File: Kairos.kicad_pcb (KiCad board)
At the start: 2 copper layers, 285 x 94.6 mm, 130 parts, among them U1 ATMEGA32U2-AU, Y1 Crystal

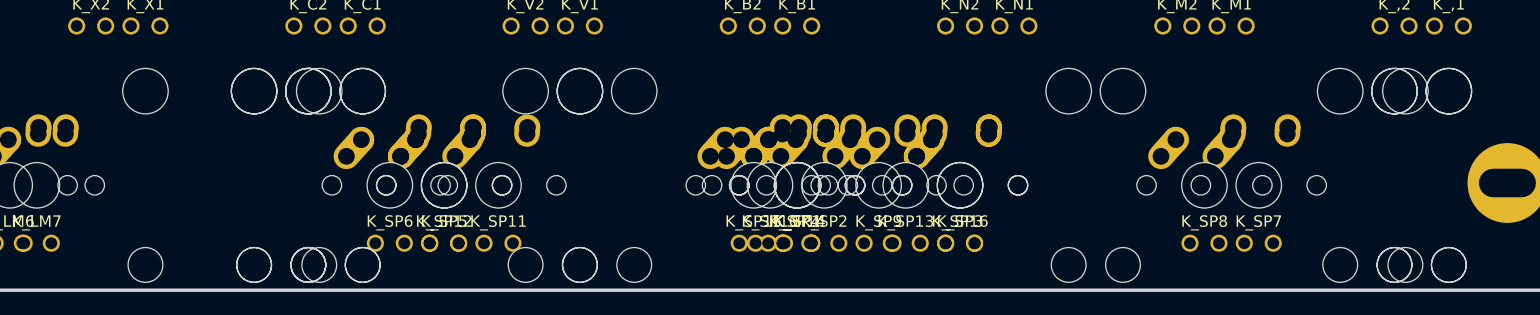
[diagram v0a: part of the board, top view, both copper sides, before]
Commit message: Removed duplicate space bars
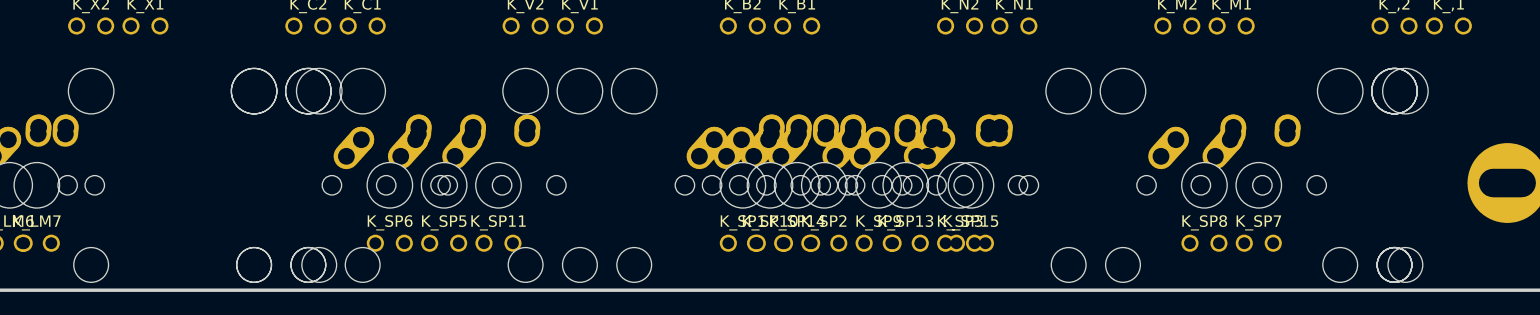
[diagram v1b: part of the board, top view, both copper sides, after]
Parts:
- removed K_SP12: MX-2.25U, MX_Alps_Hybrid:MX-2.25U
- removed K_SP16: MX-6.5U, MX_Alps_Hybrid:MX-6.5U
- removed K_SP4: MX-6U, MX_Alps_Hybrid:MX-6U
- moved K_SP1 4.76 mm to (128.6, 107.2)
- turned K_SP15 to 0 degrees

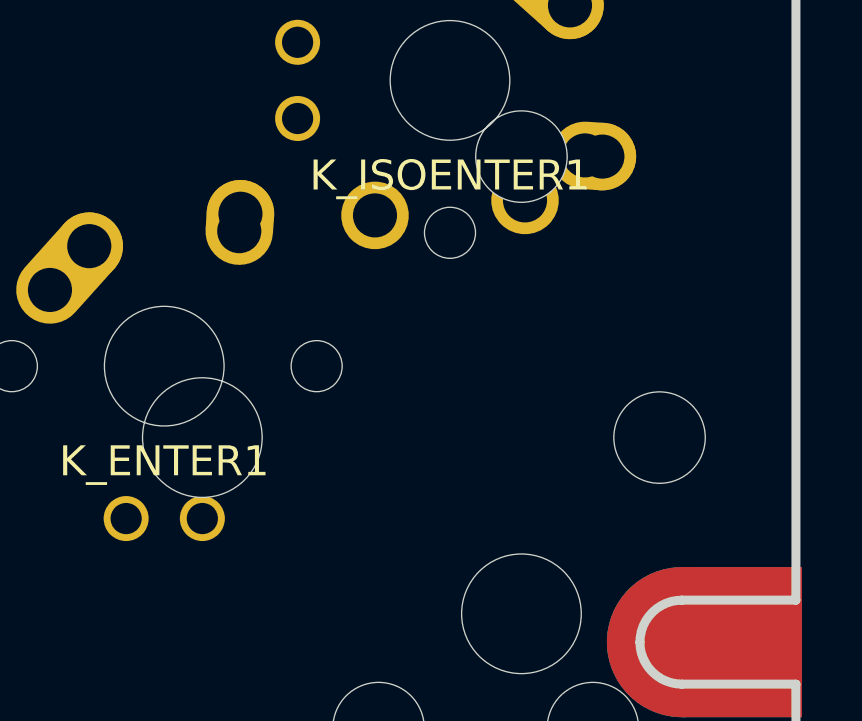
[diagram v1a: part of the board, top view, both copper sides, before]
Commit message: added split enter
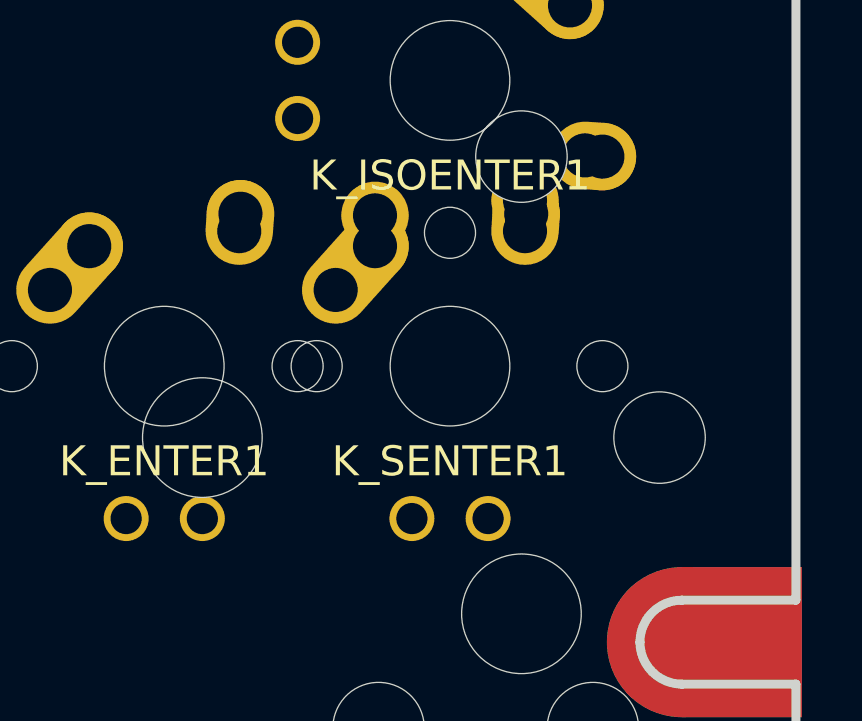
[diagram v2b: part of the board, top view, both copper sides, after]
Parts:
- added K_SENTER1: MX-1.25U, MX_Alps_Hybrid:MX-1.25U, F.Cu at (278.6, 69.1)
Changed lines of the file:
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@@
 (kicad_pcb (version 4) (host pcbnew 4.0.2-stable)
   (general
-    (links 556)
-    (no_connects 323)
+    (links 562)
+    (no_connects 327)
     (area 0 0 0 0)
     (thickness 1.6)
@@
     (tracks 34)
     (zones 0)
-    (modules 127)
+    (modules 128)
     (nets 181)
   )
@@
     (pad 4 thru_hole circle (at 1.27 5.08) (size 1.5 1.5) (drill 1.04) (layers *.Cu *.Mask)
       (net 4 LEDGND))
+    (pad "" np_thru_hole circle (at -5.08 0 48.0996) (size 1.7018 1.7018) (drill 1.7018) (layers *.Cu *.Mask))
+    (pad "" np_thru_hole circle (at 5.08 0 48.0996) (size 1.7018 1.7018) (drill 1.7018) (layers *.Cu *.Mask))
+  )
+  (module MX_Alps_Hybrid:MX-1.25U (layer F.Cu)
+    (at 278.60625 69.05625)
+    (fp_text reference K_SENTER1 (at 0 3.175) (layer F.SilkS)
+      (effects (font (size 1 1) (thickness 0.15)))
+    )
+    (fp_text value MX-1.25U (at 0 -7.9375) (layer Dwgs.User)
+      (effects (font (size 1 1) (thickness 0.15)))
+    )
+    (fp_line (start 5 -7) (end 7 -7) (layer Dwgs.User) (width 0.15))
+    (fp_line (start 7 -7) (end 7 -5) (layer Dwgs.User) (width 0.15))
+    (fp_line (start 5 7) (end 7 7) (layer Dwgs.User) (width 0.15))
+    (fp_line (start 7 7) (end 7 5) (layer Dwgs.User) (width 0.15))
+    (fp_line (start -7 5) (end -7 7) (layer Dwgs.User) (width 0.15))
+    (fp_line (start -7 7) (end -5 7) (layer Dwgs.User) (width 0.15))
+    (fp_line (start -5 -7) (end -7 -7) (layer Dwgs.User) (width 0.15))
+    (fp_line (start -7 -7) (end -7 -5) (layer Dwgs.User) (width 0.15))
+    (fp_line (start -11.90625 -9.525) (end 11.90625 -9.525) (layer Dwgs.User) (width 0.15))
+    (fp_line (start 11.90625 -9.525) (end 11.90625 9.525) (layer Dwgs.User) (width 0.15))
+    (fp_line (start -11.90625 9.525) (end 11.90625 9.525) (layer Dwgs.User) (width 0.15))
+    (fp_line (start -11.90625 9.525) (end -11.90625 -9.525) (layer Dwgs.User) (width 0.15))
+    (pad 2 thru_hole oval (at 2.5 -4.5 86.0548) (size 2.831378 2.25) (drill 1.47 (offset 0.290689 0)) (layers *.Cu *.Mask)
+      (net 24 ROW5))
+    (pad 2 thru_hole circle (at 2.54 -5.08) (size 2.25 2.25) (drill 1.47) (layers *.Cu *.Mask)
+      (net 24 ROW5))
+    (pad 1 thru_hole oval (at -3.81 -2.54 48.09963212) (size 4.211556 2.25) (drill 1.47 (offset 0.980778 0)) (layers *.Cu *.Mask)
+      (net 55 "Net-(DENTER1-Pad1)"))
+    (pad "" np_thru_hole circle (at 0 0) (size 3.9878 3.9878) (drill 3.9878) (layers *.Cu *.Mask))
+    (pad 1 thru_hole circle (at -2.5 -4) (size 2.25 2.25) (drill 1.47) (layers *.Cu *.Mask)
+      (net 55 "Net-(DENTER1-Pad1)"))
+    (pad 3 thru_hole circle (at -1.27 5.08) (size 1.5 1.5) (drill 1.04) (layers *.Cu *.Mask)
+      (net 56 "Net-(K_ENTER1-Pad3)"))
+    (pad 4 thru_hole circle (at 1.27 5.08) (size 1.5 1.5) (drill 1.04) (layers *.Cu *.Mask)
+      (net 4 LEDGND))

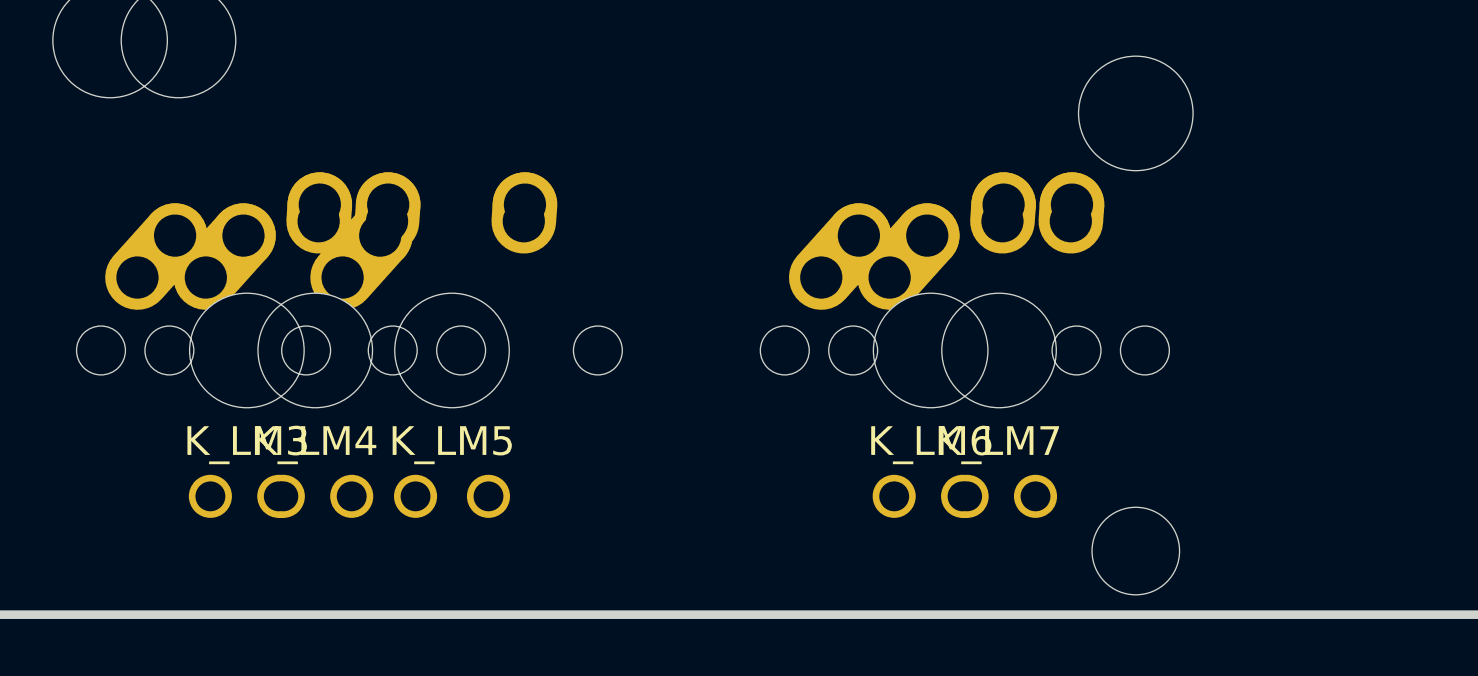
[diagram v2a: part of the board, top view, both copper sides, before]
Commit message: more left mods added
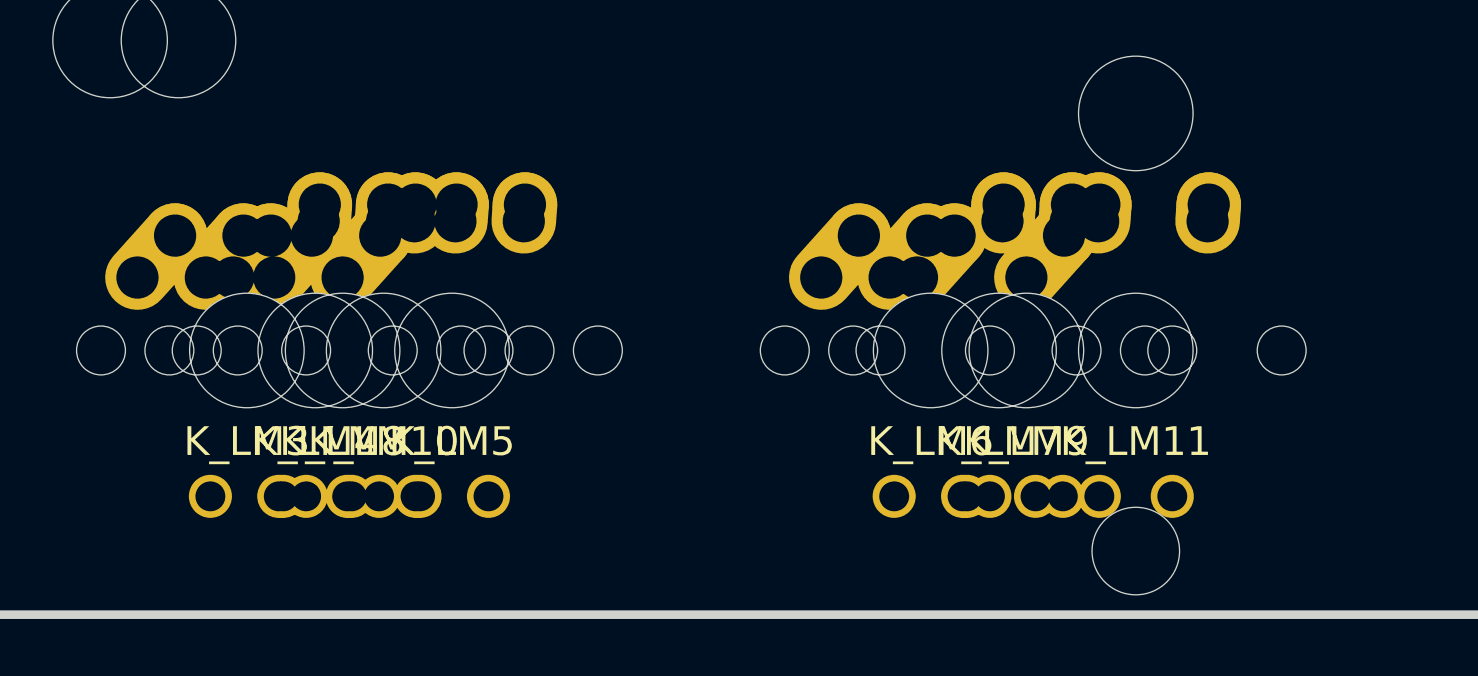
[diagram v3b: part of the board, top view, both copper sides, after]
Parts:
- added K_LM10: MX-1.25U, MX_Alps_Hybrid:MX-1.25U, F.Cu at (45.2, 107.2)
- added K_LM11: MX-1.5U, MX_Alps_Hybrid:MX-1.5U, F.Cu at (71.4, 107.2)
- added K_LM8: MX-1U, MX_Alps_Hybrid:MX-1U, F.Cu at (43.8, 107.2)
- added K_LM9: MX-1.5U, MX_Alps_Hybrid:MX-1.5U, F.Cu at (67.6, 107.2)

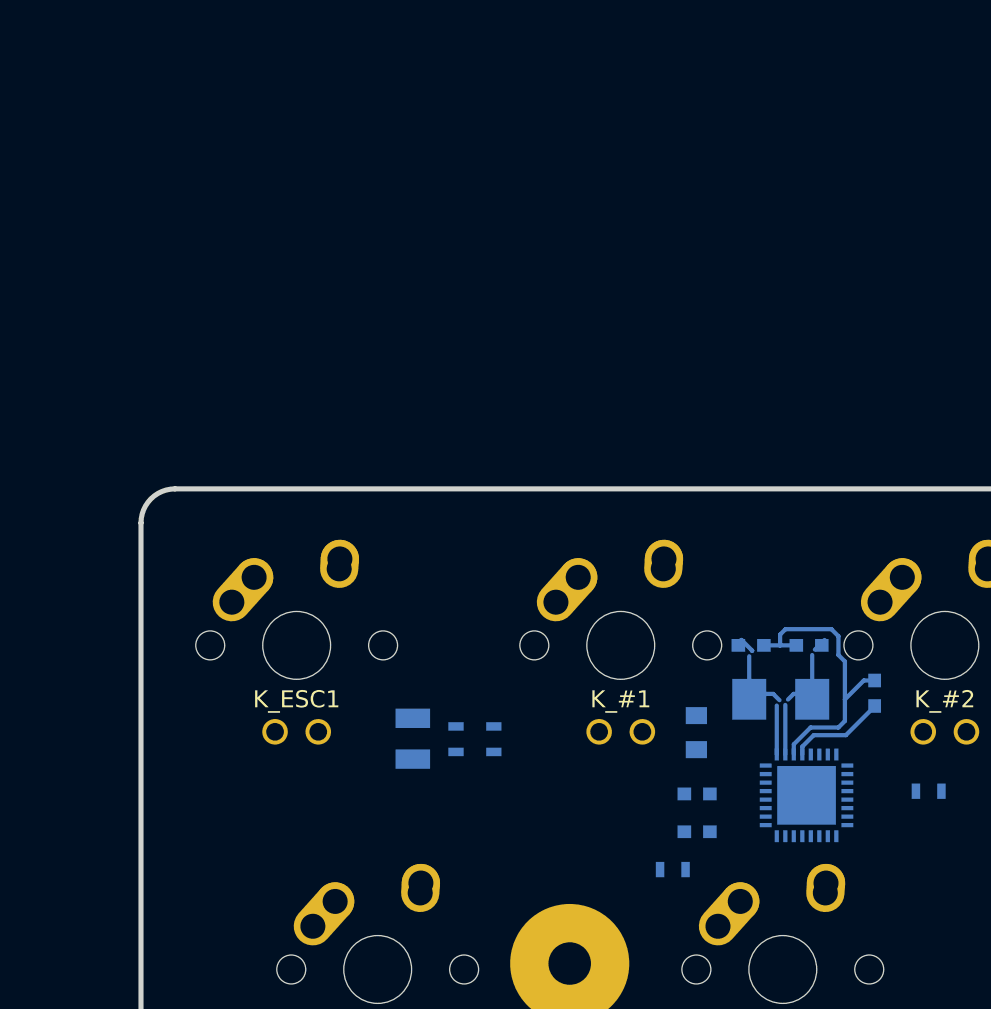
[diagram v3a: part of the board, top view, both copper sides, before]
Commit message: Add missing 1.5k resistor on LED PWM
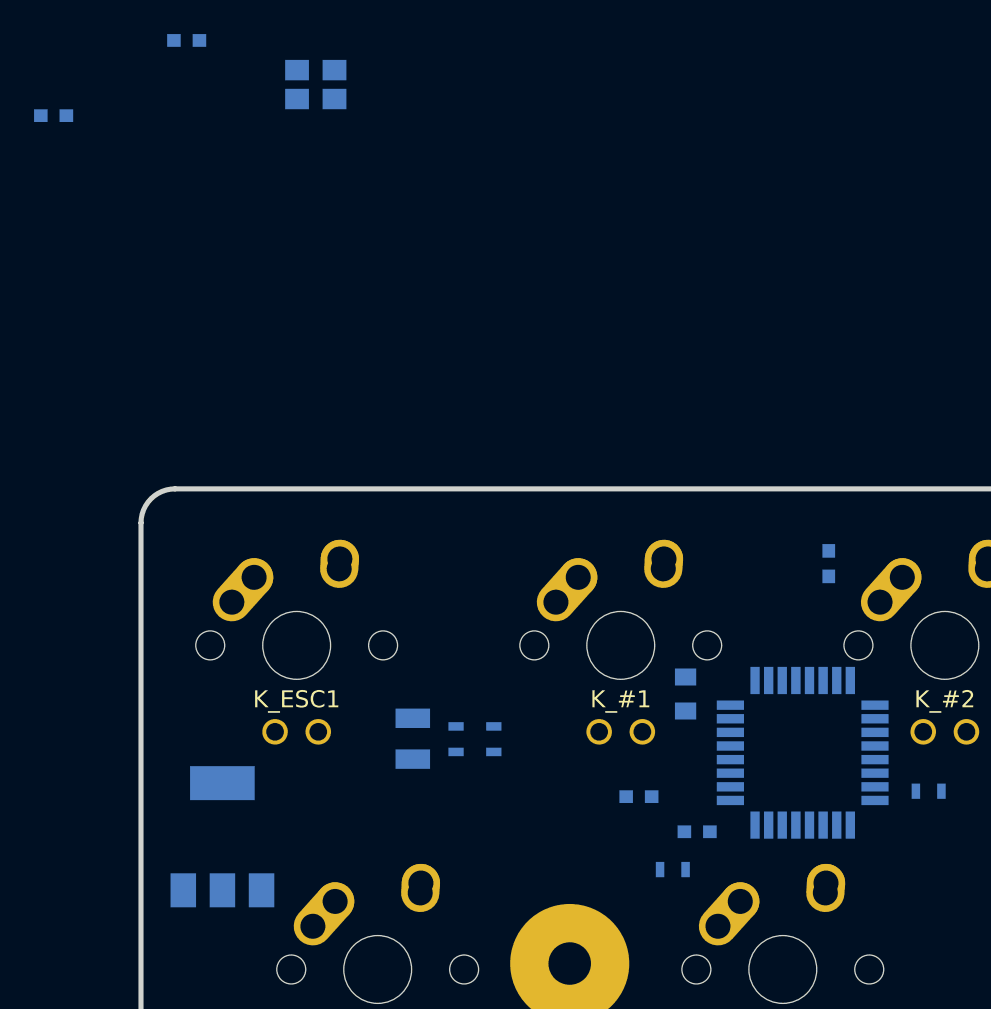
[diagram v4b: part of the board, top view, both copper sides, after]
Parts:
- added Q1: NSS40301MZ4T1G, TO_SOT_Packages_SMD:SOT-223-3Lead_TabPin2, B.Cu at (9.92, 42.2)
- U1: footprint Housings_DFN_QFN:QFN-32-1EP_5x5mm_Pitch0.5mm -> Housings_QFP:TQFP-32_7x7mm_Pitch0.8mm
- Y1: footprint Crystals:Crystal_SMD_5032-2pin_5.0x3.2mm -> Crystals:Crystal_SMD_3225-4pin_3.2x2.5mm
- moved C6 51.5 mm to (0.00, -0.18)
- moved C5 51.0 mm to (7.82, -4.60), turned to 0 degrees
- moved Y1 45.3 mm to (15.4, -2.01)
- moved C3 8.08 mm to (45.6, 26.1)
- moved C2 3.42 mm to (34.4, 39.8)
- moved U1 2.51 mm to (44.0, 37.3)
- moved C4 2.36 mm to (37.1, 33.8)
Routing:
- net GND: track 17.8 -> 0.00 mm
- net Net-(C6-Pad1): track 8.11 -> 0.00 mm
- net Net-(C5-Pad1): track 8.04 -> 0.00 mm
- net +5V: track 5.72 -> 0.00 mm
